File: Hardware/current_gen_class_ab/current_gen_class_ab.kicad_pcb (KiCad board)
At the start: 2 copper layers, 22 parts, among them J1 Conn_Coaxial, J2 Conn_Coaxial, J3 Conn_01x01_Socket, J4 Conn_01x01_Socket, J5 Conn_01x01_Socket, Q1 PMOS, Q2 NMOS, Q3 NMOS, Q4 PMOS, U1 Opamp_Dual, U2 Opamp_Dual

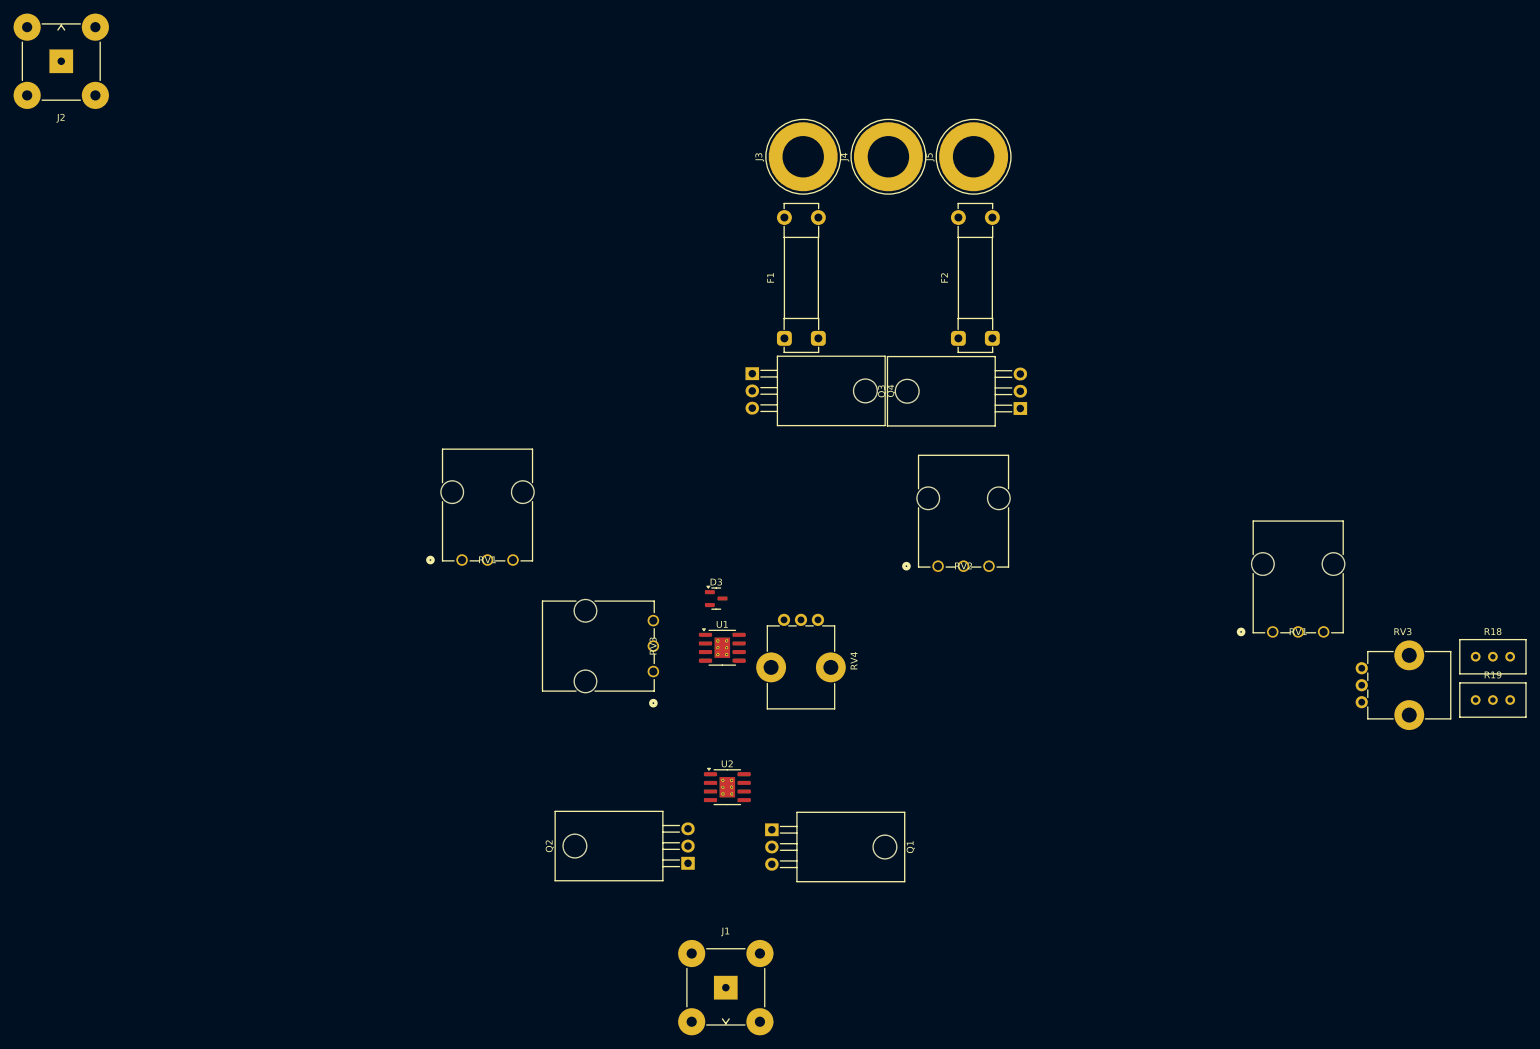
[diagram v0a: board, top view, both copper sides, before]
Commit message: routed main amp
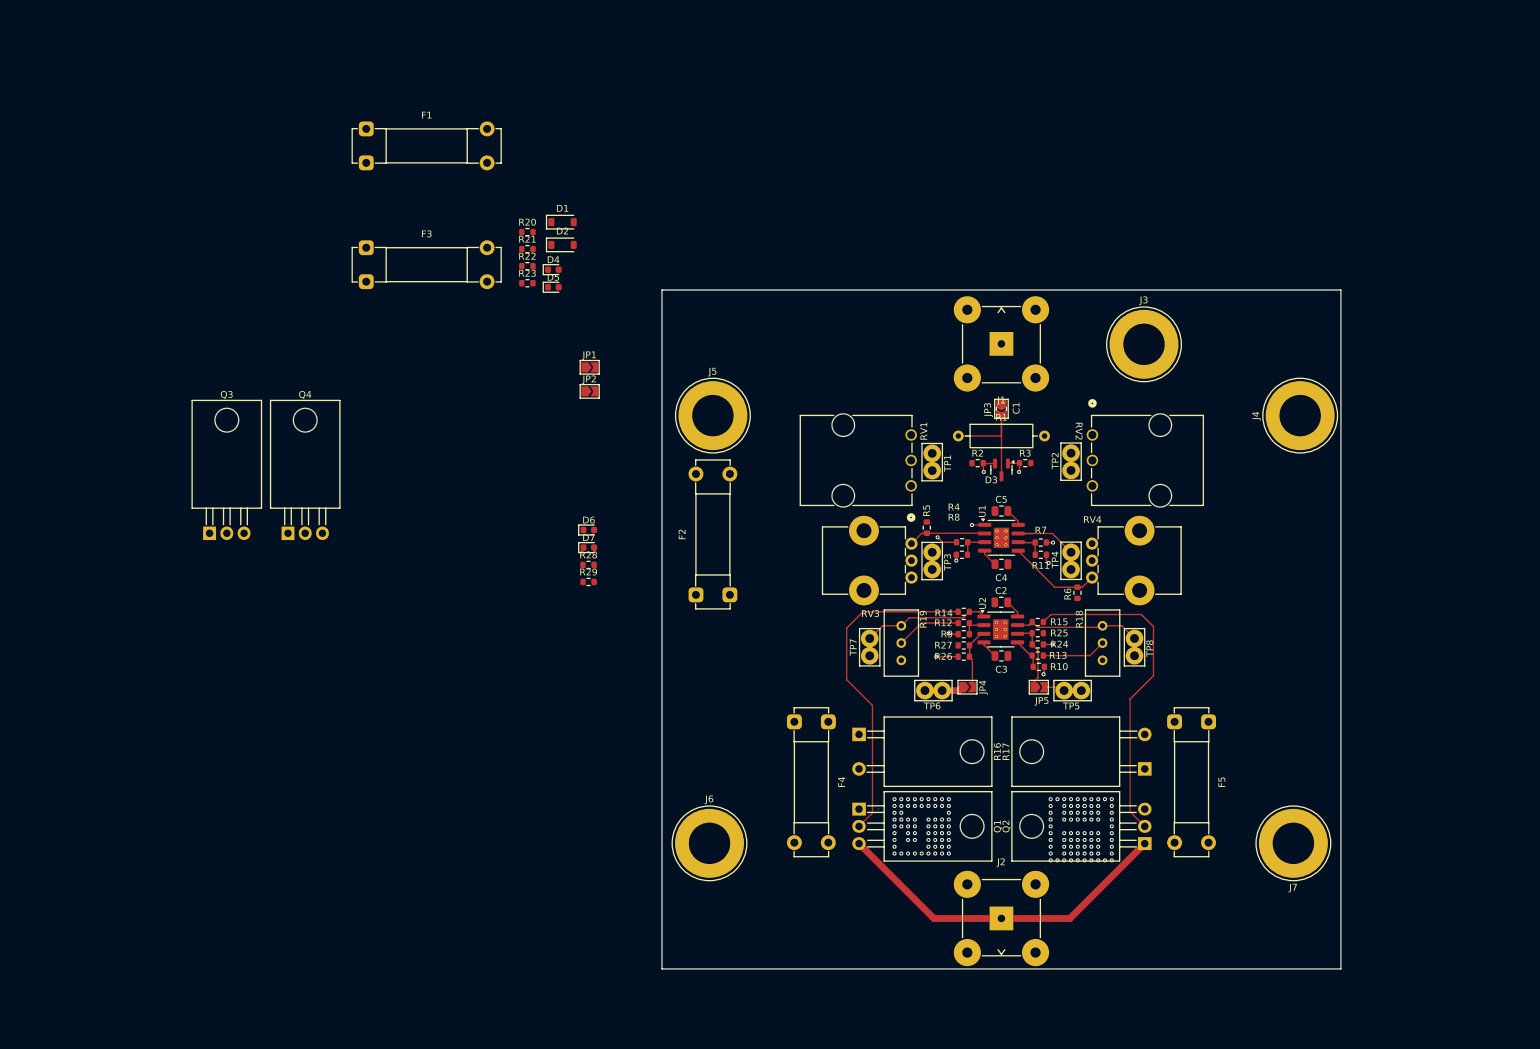
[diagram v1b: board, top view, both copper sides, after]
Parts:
- removed the RV1 at (79.5, 99.8)
- removed the RV1 at (199.0, 110.4)
- removed the RV3 at (107.7, 116.2)
- removed the RV3 at (212.1, 120.7)
- added C1: 1u, Capacitor_SMD:C_0805_2012Metric, F.Cu at (159.0, 77.5)
- added C2: 1u, Capacitor_SMD:C_0805_2012Metric, F.Cu at (159.0, 106.0)
- added C3: 1u, Capacitor_SMD:C_0805_2012Metric, F.Cu at (159.0, 113.9)
- added C4: 1u, Capacitor_SMD:C_0805_2012Metric, F.Cu at (159.0, 100.4)
- added C5: 1u, Capacitor_SMD:C_0805_2012Metric, F.Cu at (159.0, 92.6)
- added D1: D_Zener, Diode_SMD:D_SOD-123, F.Cu at (94.3, 50.0)
- added D2: D_Zener, Diode_SMD:D_SOD-123, F.Cu at (94.3, 53.4)
- added D4: LED, Diode_SMD:D_0603_1608Metric, F.Cu at (93.0, 57.0)
- added D5: LED, Diode_SMD:D_0603_1608Metric, F.Cu at (93.0, 59.6)
- added D6: LED, Diode_SMD:D_0603_1608Metric, F.Cu at (98.2, 95.3)
- added D7: LED, Diode_SMD:D_0603_1608Metric, F.Cu at (98.2, 97.9)
- added F3: Fuse, Fuse:Fuseholder_Clip-5x20mm_Bel_FC-203-22_Lateral_P17.80x5.00mm_D1.17mm_Horizontal, F.Cu at (65.4, 53.8)
- added F4: Fuse, Fuse:Fuseholder_Clip-5x20mm_Bel_FC-203-22_Lateral_P17.80x5.00mm_D1.17mm_Horizontal, F.Cu at (133.5, 123.6)
- added F5: Fuse, Fuse:Fuseholder_Clip-5x20mm_Bel_FC-203-22_Lateral_P17.80x5.00mm_D1.17mm_Horizontal, F.Cu at (189.5, 123.6)
- added J6: Conn_01x01_Socket, Connector:Banana_Jack_1Pin, F.Cu at (116.0, 141.5)
- added J7: Conn_01x01_Socket, Connector:Banana_Jack_1Pin, F.Cu at (202.0, 141.5)
- added JP1: Jumper_2_Open, Jumper:SolderJumper-2_P1.3mm_Open_TrianglePad1.0x1.5mm, F.Cu at (98.3, 71.4)
- added JP2: Jumper_2_Open, Jumper:SolderJumper-2_P1.3mm_Open_TrianglePad1.0x1.5mm, F.Cu at (98.3, 74.9)
- added JP3: Jumper_2_Open, Jumper:SolderJumper-2_P1.3mm_Open_TrianglePad1.0x1.5mm, F.Cu at (159.0, 77.5)
- added JP4: Jumper_2_Open, Jumper:SolderJumper-2_P1.3mm_Open_TrianglePad1.0x1.5mm, F.Cu at (154.0, 118.5)
- added JP5: Jumper_2_Open, Jumper:SolderJumper-2_P1.3mm_Open_TrianglePad1.0x1.5mm, F.Cu at (164.5, 118.5)
- added R1: 50, Resistor_THT:R_Axial_DIN0309_L9.0mm_D3.2mm_P12.70mm_Horizontal, F.Cu at (152.7, 81.5)
- added R10: 1k, Resistor_SMD:R_0603_1608Metric, F.Cu at (164.5, 115.5)
- added R11: 100k, Resistor_SMD:R_0603_1608Metric, F.Cu at (164.8, 99.0)
- added R12: 92k, Resistor_SMD:R_0603_1608Metric, F.Cu at (153.4, 109.0)
- added R13: 92k, Resistor_SMD:R_0603_1608Metric, F.Cu at (164.3, 113.8)
- added R14: 10, Resistor_SMD:R_0603_1608Metric, F.Cu at (153.5, 107.4)
- added R15: 10, Resistor_SMD:R_0603_1608Metric, F.Cu at (164.3, 108.9)
- added R16: 5R, Package_TO_SOT_THT:TO-220-2_Horizontal_TabDown, F.Cu at (138.0, 125.5)
- added R17: 5R, Package_TO_SOT_THT:TO-220-2_Horizontal_TabDown, F.Cu at (180.1, 130.5)
- added R2: 92k, Resistor_SMD:R_0603_1608Metric, F.Cu at (155.5, 85.5)
- added R20: 92k, Resistor_SMD:R_0603_1608Metric, F.Cu at (89.2, 51.5)
- added R21: 92k, Resistor_SMD:R_0603_1608Metric, F.Cu at (89.2, 54.0)
- added R22: 1k, Resistor_SMD:R_0603_1608Metric, F.Cu at (89.2, 56.5)
- added R23: 1k, Resistor_SMD:R_0603_1608Metric, F.Cu at (89.2, 59.0)
- added R24: 1k, Resistor_SMD:R_0603_1608Metric, F.Cu at (164.3, 112.2)
- added R25: 27k, Resistor_SMD:R_0603_1608Metric, F.Cu at (164.3, 110.5)
- added R26: 1k, Resistor_SMD:R_0603_1608Metric, F.Cu at (153.5, 114.0)
- added R27: 27k, Resistor_SMD:R_0603_1608Metric, F.Cu at (153.4, 112.3)
- added R28: 1k, Resistor_SMD:R_0603_1608Metric, F.Cu at (98.2, 100.5)
- added R29: 1k, Resistor_SMD:R_0603_1608Metric, F.Cu at (98.2, 103.0)
- added R3: 92k, Resistor_SMD:R_0603_1608Metric, F.Cu at (162.5, 85.5)
- added R4: 100k, Resistor_SMD:R_0603_1608Metric, F.Cu at (153.2, 97.2)
- added R5: 1k, Resistor_SMD:R_0603_1608Metric, F.Cu at (148.0, 95.0)
- added R6: 1k, Resistor_SMD:R_0603_1608Metric, F.Cu at (170.2, 104.6)
- added R7: 100k, Resistor_SMD:R_0603_1608Metric, F.Cu at (164.8, 97.2)
- added R8: 100k, Resistor_SMD:R_0603_1608Metric, F.Cu at (153.2, 99.0)
- added R9: 1k, Resistor_SMD:R_0603_1608Metric, F.Cu at (153.4, 110.7)
- added RV1: 10k, footprints:POT_P120PK-x25_TTE, F.Cu at (145.7, 88.8)
- added RV3: 10k, Potentiometer_THT:Potentiometer_Bourns_PTV09A-1_Single_Vertical, F.Cu at (145.8, 97.3)
- added TP1: TestPoint, TestPoint:TestPoint_Bridge_Pitch2.54mm_Drill1.3mm, F.Cu at (148.8, 86.6)
- added TP2: TestPoint, TestPoint:TestPoint_Bridge_Pitch2.54mm_Drill1.3mm, F.Cu at (169.2, 84.0)
- added TP3: TestPoint, TestPoint:TestPoint_Bridge_Pitch2.54mm_Drill1.3mm, F.Cu at (148.8, 101.2)
- added TP4: TestPoint, TestPoint:TestPoint_Bridge_Pitch2.54mm_Drill1.3mm, F.Cu at (169.2, 98.6)
- added TP5: TestPoint, TestPoint:TestPoint_Bridge_Pitch2.54mm_Drill1.3mm, F.Cu at (168.2, 119.0)
- added TP6: TestPoint, TestPoint:TestPoint_Bridge_Pitch2.54mm_Drill1.3mm, F.Cu at (147.7, 119.0)
- added TP7: TestPoint, TestPoint:TestPoint_Bridge_Pitch2.54mm_Drill1.3mm, F.Cu at (139.6, 113.9)
- added TP8: TestPoint, TestPoint:TestPoint_Bridge_Pitch2.54mm_Drill1.3mm, F.Cu at (178.6, 113.9)
- moved J2 187.4 mm to (159.0, 152.6), turned to 180 degrees
- moved Q3 120.8 mm to (42.4, 95.8), turned to 0 degrees
- moved J1 103.1 mm to (159.0, 67.9), turned to 0 degrees
- moved R19 90.3 mm to (144.2, 109.5), turned to 90 degrees
- moved Q4 72.3 mm to (53.9, 95.8), turned to 0 degrees
- moved J4 71.6 mm to (203.0, 78.5)
- moved F1 68.9 mm to (65.4, 36.3), turned to 0 degrees
- moved Q2 67.3 mm to (180.1, 141.5)
- moved R18 60.2 mm to (173.9, 109.5), turned to 90 degrees
- moved J3 57.3 mm to (180.0, 68.0), turned to 0 degrees
- moved J5 54.1 mm to (116.5, 78.5), turned to 0 degrees
- moved F2 54.1 mm to (114.0, 104.9)
- moved U2 46.5 mm to (158.9, 110.0)
- moved D3 46.1 mm to (159.0, 86.5), turned to -90 degrees
- moved RV4 45.8 mm to (172.3, 102.3), turned to 0 degrees
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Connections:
- J4 pad 1: GND -> Net-(J4-Pin_1)
- Q3 pad 1: Net-(JP2-A) -> -15V
- Q3 pad 3: -15V -> Net-(JP2-A)
- R18 pad 1: Net-(R13-Pad1) -> Net-(R15-Pad1)
- R18 pad 2: Net-(R15-Pad1) -> Net-(R13-Pad1)
- R19 pad 1: Net-(R12-Pad1) -> Net-(R14-Pad1)
- R19 pad 2: Net-(R14-Pad1) -> Net-(R12-Pad1)
- RV4 pad 1: unconnected-(RV4-Pad1) -> Net-(U1B-+)
- RV4 pad 2: Net-(U2B--) -> Net-(R24-Pad2)
- RV4 pad 3: Net-(U1B-+) -> unconnected-(RV4-Pad3)
- U1 pad 1: Net-(U2A-+) -> Net-(R26-Pad2)
- U1 pad 7: Net-(U2B--) -> Net-(R24-Pad2)
- U2 pad 3: Net-(U2A-+) -> Net-(JP4-B)
- U2 pad 6: Net-(U2B--) -> Net-(JP5-A)
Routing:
- net Net-(J2-In): track 0.00 -> 51.2 mm
- net Net-(Q2-G): track 0.00 -> 49.2 mm
- net Net-(Q1-G): track 0.00 -> 49.0 mm
- net Net-(JP4-A): track 0.00 -> 49.0 mm, vias 0 -> 1
- net Net-(JP5-B): track 0.00 -> 48.2 mm, vias 0 -> 1
- net Net-(D3-K-Pad1): track 0.00 -> 35.5 mm, vias 0 -> 2
- net Net-(R26-Pad2): track 0.00 -> 31.9 mm, vias 0 -> 2
- net Net-(R24-Pad2): track 0.00 -> 30.9 mm, vias 0 -> 1
- net Net-(D3-A): track 0.00 -> 30.7 mm, vias 0 -> 2
- net Net-(R4-Pad2): track 0.00 -> 19.3 mm, vias 0 -> 1
- net Net-(R7-Pad2): track 0.00 -> 18.8 mm, vias 0 -> 1
- net Net-(R14-Pad1): track 0.00 -> 18.7 mm
- net Net-(R15-Pad1): track 0.00 -> 18.6 mm
- net Net-(JP3-B): track 0.00 -> 18.4 mm
- net Net-(U1B-+): track 0.00 -> 13.7 mm
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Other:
- board outline added: 100 x 100 mm
- copper layers 2 -> 4
- board text added: "sig --- gnd --- pwr / sig --- gnd"

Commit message: routed power started adding stitching and thermal vias
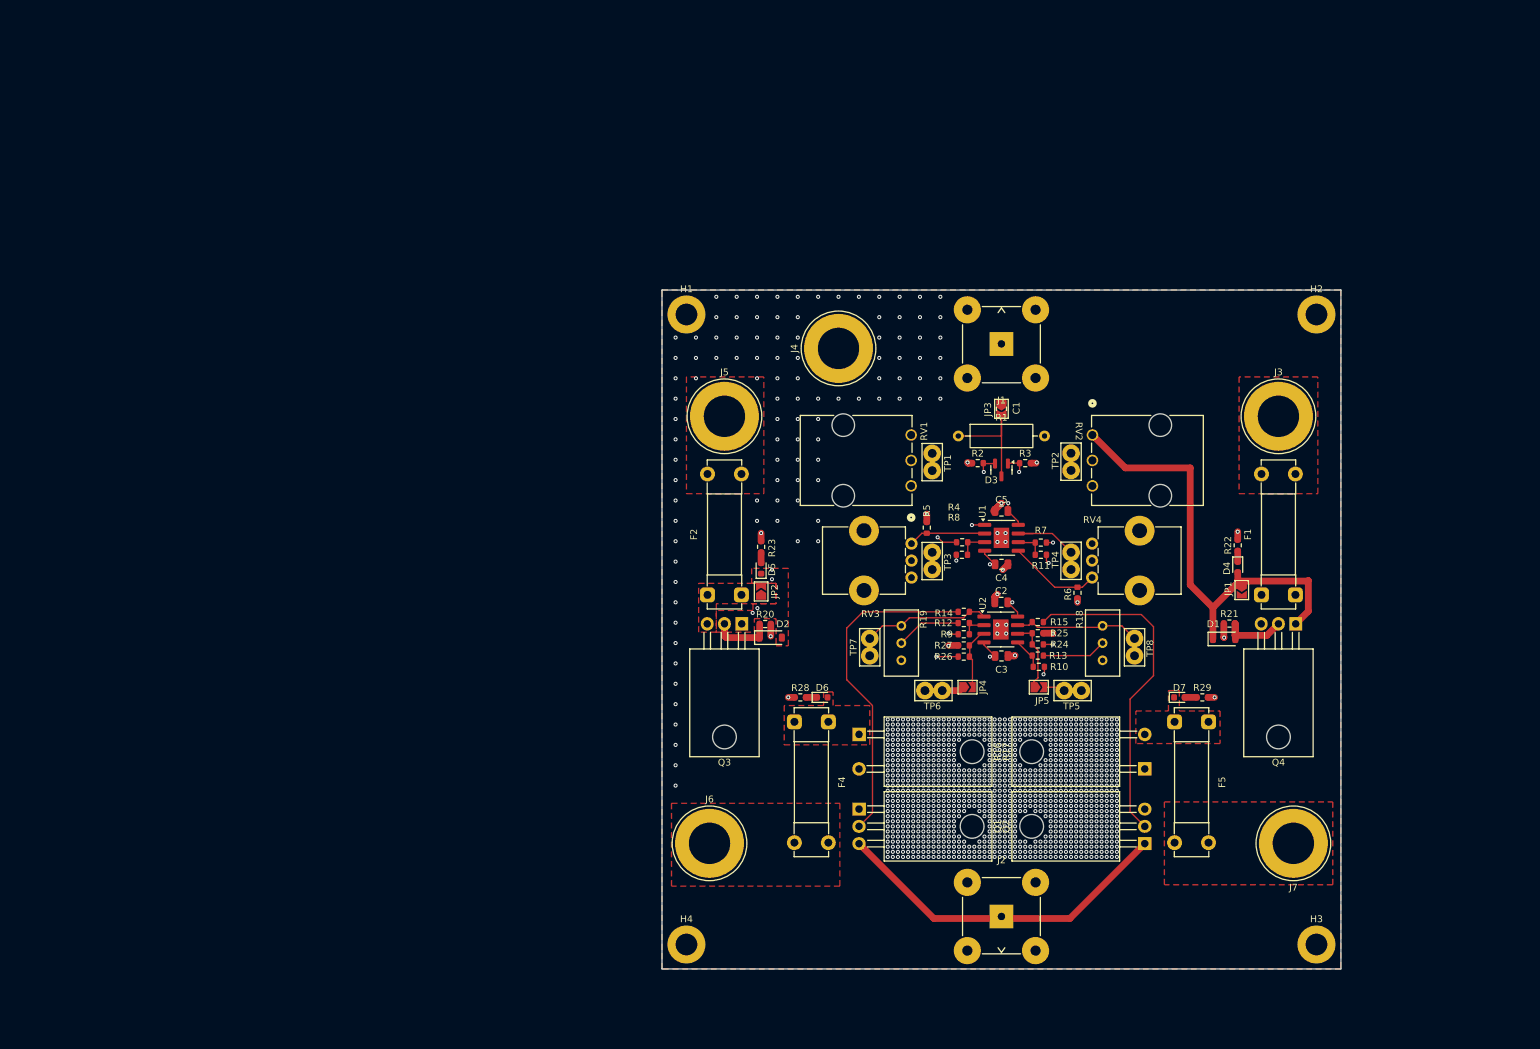
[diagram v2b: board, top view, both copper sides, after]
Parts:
- removed F3: Fuse, Fuse:Fuseholder_Clip-5x20mm_Bel_FC-203-22_Lateral_P17.80x5.00mm_D1.17mm_Horizontal
- added H1: MountingHole_Pad, MountingHole:MountingHole_3.2mm_M3_DIN965_Pad, F.Cu at (112.6, 63.6)
- added H2: MountingHole_Pad, MountingHole:MountingHole_3.2mm_M3_DIN965_Pad, F.Cu at (205.4, 63.6)
- added H3: MountingHole_Pad, MountingHole:MountingHole_3.2mm_M3_DIN965_Pad, F.Cu at (205.4, 156.4)
- added H4: MountingHole_Pad, MountingHole:MountingHole_3.2mm_M3_DIN965_Pad, F.Cu at (112.6, 156.4)
- moved Q4 149.0 mm to (202.3, 109.2), turned to 180 degrees
- moved F1 148.7 mm to (197.3, 104.9), turned to 90 degrees
- moved R21 117.2 mm to (192.6, 109.1)
- moved D1 115.2 mm to (191.8, 111.4)
- moved R22 112.4 mm to (193.8, 97.6), turned to 90 degrees
- moved D4 109.9 mm to (193.8, 100.8), turned to -90 degrees
- moved JP1 101.5 mm to (194.4, 104.2), turned to -90 degrees
- moved R29 92.0 mm to (188.6, 120.0)
- moved D7 89.8 mm to (185.2, 120.0)
- moved Q3 79.5 mm to (120.7, 109.2), turned to 180 degrees
- moved J4 68.7 mm to (135.0, 68.6)
- moved R20 67.5 mm to (124.2, 109.2)
- moved D2 65.5 mm to (125.0, 111.2)
- moved R23 51.9 mm to (123.6, 97.8), turned to 90 degrees
- moved D5 51.5 mm to (123.6, 101.0), turned to 90 degrees
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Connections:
- J4 pad 1: Net-(J4-Pin_1) -> GND
- U1 pad 9: (no net) -> GND
- U2 pad 9: (no net) -> GND
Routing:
- net +15V: track 5.37 -> 113.1 mm, vias 0 -> 2
- net -15V: track 5.29 -> 102.9 mm, vias 0 -> 6
- net GND: track 0.00 -> 21.0 mm, vias 0 -> 1291
- net Net-(D1-A): track 0.00 -> 11.1 mm
- net Net-(D2-K): track 0.00 -> 9.03 mm
- net Net-(JP5-B): track 48.2 -> 50.8 mm
- net Net-(D7-A): track 0.00 -> 1.76 mm
- net Net-(D6-K): track 0.00 -> 1.61 mm
- net Net-(D4-K): track 0.00 -> 1.59 mm
- net Net-(D5-A): track 0.00 -> 1.55 mm
- net Net-(JP4-A): track 49.0 -> 49.8 mm
- net (no net): vias 144 -> 0
- added copper zone on F.Cu, net +10V
- added copper zone on F.Cu, net -10V
- added copper zone on F.Cu, net -15V
- added copper zone on B.Cu, net GND
- added copper zone on F.Cu, net GND
- added copper zone on In1.Cu, net GND
- added copper zone on In2.Cu, net GND
- added copper zone on F.Cu, net Net-(J3-Pin_1)
- added copper zone on F.Cu, net Net-(J5-Pin_1)
- added copper zone on F.Cu, net Net-(J6-Pin_1)
- added copper zone on F.Cu, net Net-(J7-Pin_1)
- added copper zone on In2.Cu, net Net-(JP1-B)
- added copper zone on F.Cu, net Net-(JP2-A)
